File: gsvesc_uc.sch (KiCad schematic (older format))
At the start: 13 parts, among them U1 STM32F405RGTx, Y1 ABM3B 8MHz

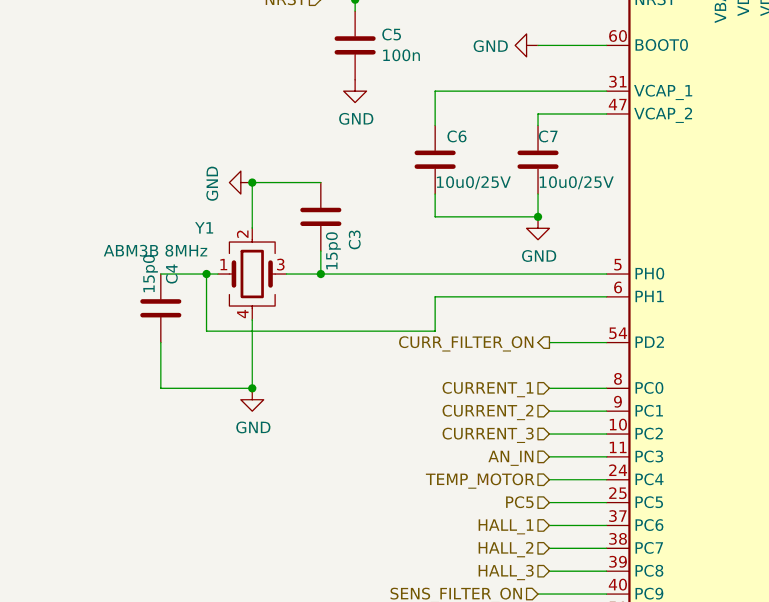
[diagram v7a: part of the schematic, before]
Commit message: einige Bauteile geändert, so dass sie Basic Parts bei JLC sind
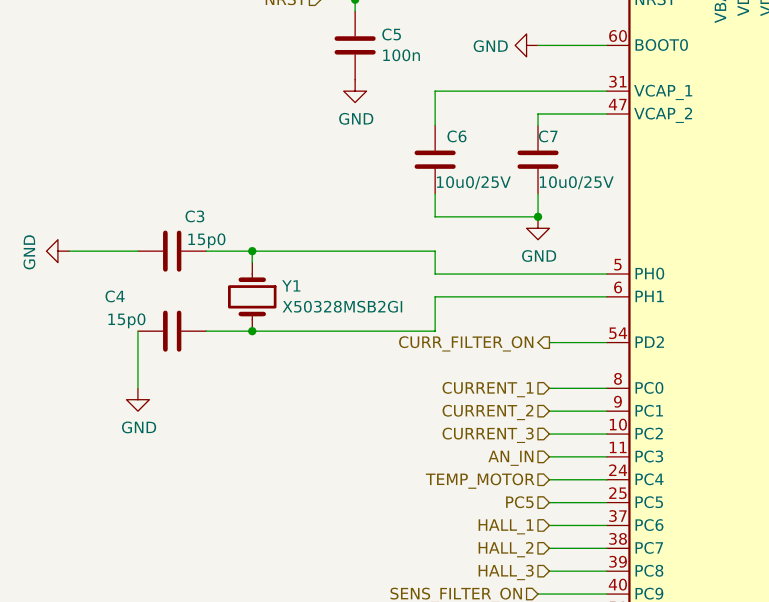
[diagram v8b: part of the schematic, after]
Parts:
- removed Y1: ABM3B 8MHz, Crystal:Crystal_SMD_5032-4Pin_5.0x3.2mm, symbol Device:Crystal_GND24
- added Y1: X50328MSB2GI, Crystal:Crystal_SMD_5032-2Pin_5.0x3.2mm, symbol Device:Crystal
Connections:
- net GND: now also C4.2; no longer C4.1
- net at C3.1, U1.5 (PH0): now also Y1.1
- net at U1.6 (PH1): now also C4.1, Y1.2; no longer C4.2
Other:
- moved on the sheet: C3, C4
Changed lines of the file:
@@
 Wire Wire Line
 	3450 5800 3200 5800
-$Comp
-L Device:Crystal_GND24 Y1
-U 1 1 5C00BFEF
-P 1900 3800
-F 0 "Y1" H 1650 4000 50  0000 L CNN
-F 1 "ABM3B 8MHz" H 1250 3900 50  0000 L CNN
-F 2 "Crystal:Crystal_SMD_5032-4Pin_5.0x3.2mm" H 1900 3800 50  0001 C CNN
-F 3 "~" H 1900 3800 50  0001 C CNN
-	1    1900 3800
-	1    0    0    -1
-$EndComp
-Wire Wire Line
-	1750 3800 1700 3800
-Wire Wire Line
-	1700 3800 1700 4050
 Wire Wire Line
 	2700 3900 3450 3900
@@
 L Device:C C3
 U 1 1 5C0116B6
-P 2200 3550
-F 0 "C3" V 2050 3650 50  0000 C CNN
-F 1 "15p0" V 2150 3700 50  0000 C CNN
-F 2 "Capacitor_SMD:C_0805_2012Metric" H 2238 3400 50  0001 C CNN
-F 3 "~" H 2200 3550 50  0001 C CNN
-	1    2200 3550
-	-1   0    0    1
+P 1550 3700
+F 0 "C3" V 1400 3800 50  0000 C CNN
+F 1 "15p0" V 1500 3850 50  0000 C CNN
+F 2 "Capacitor_SMD:C_0805_2012Metric" H 1588 3550 50  0001 C CNN
+F 3 "~" H 1550 3700 50  0001 C CNN
+	1    1550 3700
+	0    1    1    0
 $EndComp
 $Comp
 L Device:C C4
 U 1 1 5C01170C
-P 1500 3950
-F 0 "C4" V 1450 3800 50  0000 C CNN
-F 1 "15p0" V 1550 3800 50  0000 C CNN
-F 2 "Capacitor_SMD:C_0805_2012Metric" H 1538 3800 50  0001 C CNN
-F 3 "~" H 1500 3950 50  0001 C CNN
-	1    1500 3950
-	-1   0    0    1
+P 1550 4050
+F 0 "C4" V 1400 3800 50  0000 C CNN
+F 1 "15p0" V 1500 3850 50  0000 C CNN
+F 2 "Capacitor_SMD:C_0805_2012Metric" H 1588 3900 50  0001 C CNN
+F 3 "~" H 1550 4050 50  0001 C CNN
+	1    1550 4050
+	0    1    1    0
 $EndComp
 $Comp
@@
 L power:GND #PWR0101
 U 1 1 5C4737D3
-P 1900 4300
-F 0 "#PWR0101" H 1900 4050 50  0001 C CNN
-F 1 "GND" H 1905 4127 50  0000 C CNN
-F 2 "" H 1900 4300 50  0001 C CNN
-F 3 "" H 1900 4300 50  0001 C CNN
-	1    1900 4300
+P 1400 4300
+F 0 "#PWR0101" H 1400 4050 50  0001 C CNN
+F 1 "GND" H 1405 4127 50  0000 C CNN
+F 2 "" H 1400 4300 50  0001 C CNN
+F 3 "" H 1400 4300 50  0001 C CNN
+	1    1400 4300
 	1    0    0    -1
 $EndComp
@@
 CURR_FILTER_ON
 Wire Wire Line
-	2050 3800 2200 3800
-Wire Wire Line
-	1700 4050 2700 4050
+	1900 4050 2700 4050
 Wire Wire Line
 	2700 4050 2700 3900
 Wire Wire Line
-	1700 3800 1500 3800
-Connection ~ 1700 3800
-Wire Wire Line
-	1900 4000 1900 4300
-Wire Wire Line
-	1900 4300 1500 4300
-Wire Wire Line
-	1500 4300 1500 4100
-Connection ~ 1900 4300
-Wire Wire Line
-	2200 3700 2200 3800
-Connection ~ 2200 3800
-Wire Wire Line
-	2200 3800 3450 3800
-Wire Wire Line
-	2200 3400 1900 3400
-Wire Wire Line
-	1900 3400 1900 3600
+	1400 4300 1400 4050
+Wire Wire Line
+	1400 3700 1100 3700
 $Comp
 L power:GND #PWR0111
 U 1 1 5E360D1D
-P 1900 3400
-F 0 "#PWR0111" H 1900 3150 50  0001 C CNN
-F 1 "GND" H 1905 3227 50  0000 C CNN
-F 2 "" H 1900 3400 50  0001 C CNN
-F 3 "" H 1900 3400 50  0001 C CNN
-	1    1900 3400
-	0    1    1    0
-$EndComp
-Connection ~ 1900 3400
+P 1100 3700
+F 0 "#PWR0111" H 1100 3450 50  0001 C CNN
+F 1 "GND" H 1105 3527 50  0000 C CNN
+F 2 "" H 1100 3700 50  0001 C CNN
+F 3 "" H 1100 3700 50  0001 C CNN
+	1    1100 3700
+	0    1    1    0
+$EndComp
 Wire Wire Line
 	3450 5200 3150 5200
@@
 NoConn ~ 3450 5400
 NoConn ~ 3450 5500
+$Comp
+L Device:Crystal Y1
+U 1 1 5E9F6748
+P 1900 3900
+F 0 "Y1" V 1854 4031 50  0000 L CNN
+F 1 "X50328MSB2GI" V 1945 4031 50  0000 L CNN
+F 2 "Crystal:Crystal_SMD_5032-2Pin_5.0x3.2mm" H 1900 3900 50  0001 C CNN
+F 3 "~" H 1900 3900 50  0001 C CNN
+	1    1900 3900
+	0    1    1    0
+$EndComp
+Wire Wire Line
+	2700 3800 3450 3800
+Wire Wire Line
+	2700 3800 2700 3700
+Wire Wire Line
+	2700 3700 1900 3700
+Wire Wire Line
+	1900 3700 1900 3750
+Wire Wire Line
+	1700 4050 1900 4050
+Connection ~ 1900 4050
+Wire Wire Line
+	1700 3700 1900 3700
+Connection ~ 1900 3700
 $EndSCHEMATC
